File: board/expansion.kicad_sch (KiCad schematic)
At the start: 2 parts, among them U13 ENGINE

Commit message: Run VPA from GLUE to CPU
* delete old ENGINE_IACK line and pullup - interrupts will be autovectored
* run VPA between GLUE and CPU
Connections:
- net ~{ENGINE_IACK}: no longer names the net of U13.6 (I/O)
- no-connect marks 8 -> 9
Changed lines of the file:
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@@
+	)
+	(no_connect
+		(at 91.44 57.15)
 	)
 	(no_connect
@@
 				(hide yes)
 			)
-		)
-	)
-	(global_label "~{ENGINE_IACK}"
-		(shape input)
-		(at 91.44 57.15 180)
-		(fields_autoplaced yes)
-		(effects
-			(font
-				(size 1.27 1.27)
-			)
-			(justify right)
-		)
-		(property "Intersheetrefs" "${INTERSHEET_REFS}"
-			(at 76.42 57.15 0)
-			(effects
-				(font
-					(size 1.27 1.27)
-				)
-				(justify right)
-				(hide yes)
-			)

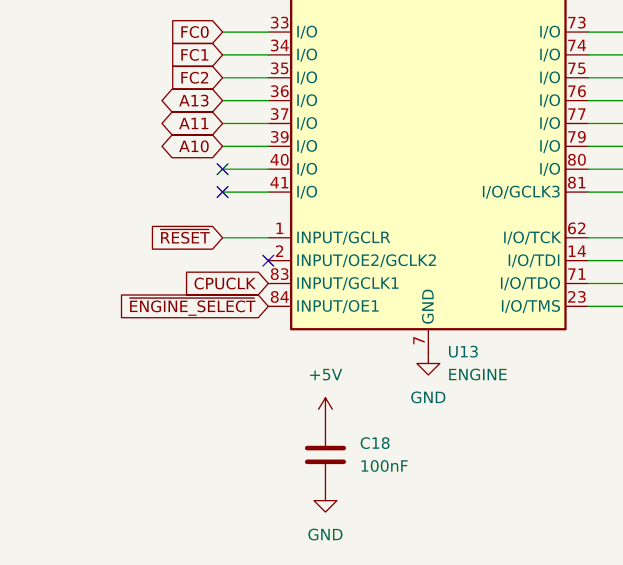
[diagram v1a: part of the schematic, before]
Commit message: CPUCLK -> SYSCLK
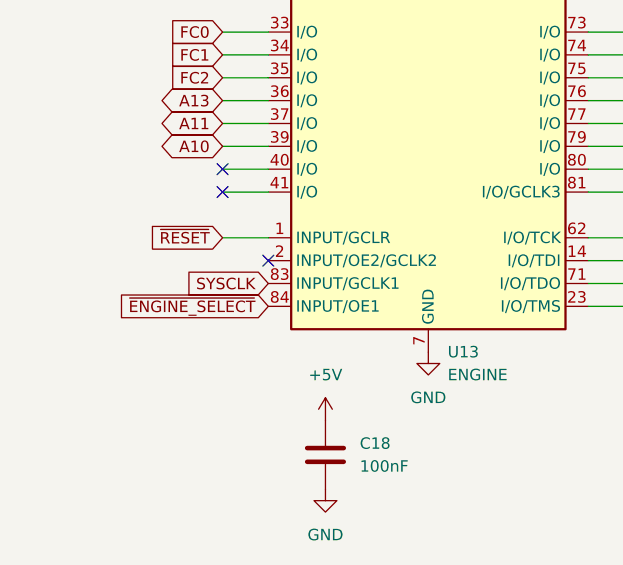
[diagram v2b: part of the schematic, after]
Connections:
- net CPUCLK renamed SYSCLK
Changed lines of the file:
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@@
 		)
 	)
-	(global_label "CPUCLK"
+	(global_label "SYSCLK"
 		(shape input)
 		(at 96.52 143.51 180)
